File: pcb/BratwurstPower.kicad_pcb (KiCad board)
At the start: 4 copper layers, 85 x 56 mm, 142 parts, among them J1 BarrelJack, J10 GPIO, J11 OTG, J2 RaspiPower, J3 USB1in, J4 USB1out, J5 I2C, J6 I2C, J7 USB2in, J8 USB2out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

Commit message: fix: change pots to 2.2kΩ
fix: part numbers
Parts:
- Q1: value AO3401A -> HL3415A
- RV1, RV2, RV3, RV4: value 2k -> 2k2
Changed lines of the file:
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@@
 			)
 		)
+		(property "LCSC" "C52923"
+			(at 0 0 -90)
+			(unlocked yes)
+			(layer "F.Fab")
+			(hide yes)
+			(effects
+				(font
+					(size 1 1)
+					(thickness 0.15)
+				)
+			)
+		)
 		(property ki_fp_filters "C_*")
 		(sheetname "Root")
@@
 			)
 		)
-		(property "LCSC" "C25890"
+		(property "LCSC" "C25879"
 			(at 0 0 90)
 			(unlocked yes)
@@
 			)
 		)
-		(property "Value" "AO3401A"
+		(property "Value" "HL3415A"
 			(at 0 2.4 90)
 			(layer "F.Fab")
@@
 			)
 		)
-		(property "Datasheet" "http://www.aosmd.com/pdfs/datasheet/AO3401A.pdf"
+		(property "Datasheet" "https://wmsc.lcsc.com/wmsc/upload/file/pdf/v2/lcsc/2407121622_hongjiacheng-HL3415A_C28646270.pdf"
 			(at 0 0 -90)
 			(unlocked yes)
@@
 			)
 		)
-		(property "LCSC" "C15127"
+		(property "LCSC" "C28646270"
 			(at 0 0 -90)
 			(unlocked yes)
@@
 			)
 		)
-		(property "Value" "2k"
+		(property "Value" "2k2"
 			(at 0 1 180)
 			(unlocked yes)
@@
 			)
 		)
-		(property "LCSC" "C128549"
+		(property "LCSC" "C145162"
 			(at 0 0 180)
 			(unlocked yes)
@@
 			)
 		)
-		(property "LCSC" "C25765"
+		(property "LCSC" "C25762"
 			(at 0 0 0)
 			(unlocked yes)
@@
 			)
 		)
-		(property "Value" "2k"
+		(property "Value" "2k2"
 			(at 0 1 90)
 			(unlocked yes)
@@
 			)
 		)
-		(property "LCSC" "C128549"
+		(property "LCSC" "C145162"
 			(at 0 0 90)
 			(unlocked yes)
@@
 			)
 		)
+		(property "LCSC" "C52923"
+			(at 0 0 90)
+			(unlocked yes)
+			(layer "F.Fab")
+			(hide yes)
+			(effects
+				(font
+					(size 1 1)
+					(thickness 0.15)
+				)
+			)
+		)
 		(property ki_fp_filters "C_*")
 		(sheetname "Root")
@@
 			)
 		)
-		(property "Value" "2k"
+		(property "Value" "2k2"
 			(at 0 1 180)
 			(unlocked yes)
@@
 			)
 		)
-		(property "LCSC" "C128549"
+		(property "LCSC" "C145162"
 			(at 0 0 180)
 			(unlocked yes)
@@
 			)
 		)
-		(property "LCSC" "C25890"
+		(property "LCSC" "C25879"
 			(at 0 0 90)
 			(unlocked yes)
@@
 			)
 		)
+		(property "LCSC" "C5446"
+			(at 0 0 90)
+			(unlocked yes)
+			(layer "F.Fab")
+			(hide yes)
+			(effects
+				(font
+					(size 1 1)
+					(thickness 0.15)
+				)
+			)
+		)
 		(property ki_fp_filters "SOT?23?3*")
 		(sheetname "Root")
@@
 			)
 		)
-		(property "LCSC" "C25765"
+		(property "LCSC" "C25762"
 			(at 0 0 90)
 			(unlocked yes)
@@
 			)
 		)
-		(property "Value" "2k"
+		(property "Value" "2k2"
 			(at 0 1 -90)
 			(unlocked yes)
@@
 			)
 		)
-		(property "LCSC" "C128549"
+		(property "LCSC" "C145162"
 			(at 0 0 -90)
 			(unlocked yes)
@@
 			)
 		)
-		(property "LCSC" "C25765"
+		(property "LCSC" "C25762"
 			(at 0 0 -90)
 			(unlocked yes)
@@
 			)
 		)
-		(property "LCSC" "C25765"
+		(property "LCSC" "C25762"
 			(at 0 0 0)
 			(unlocked yes)

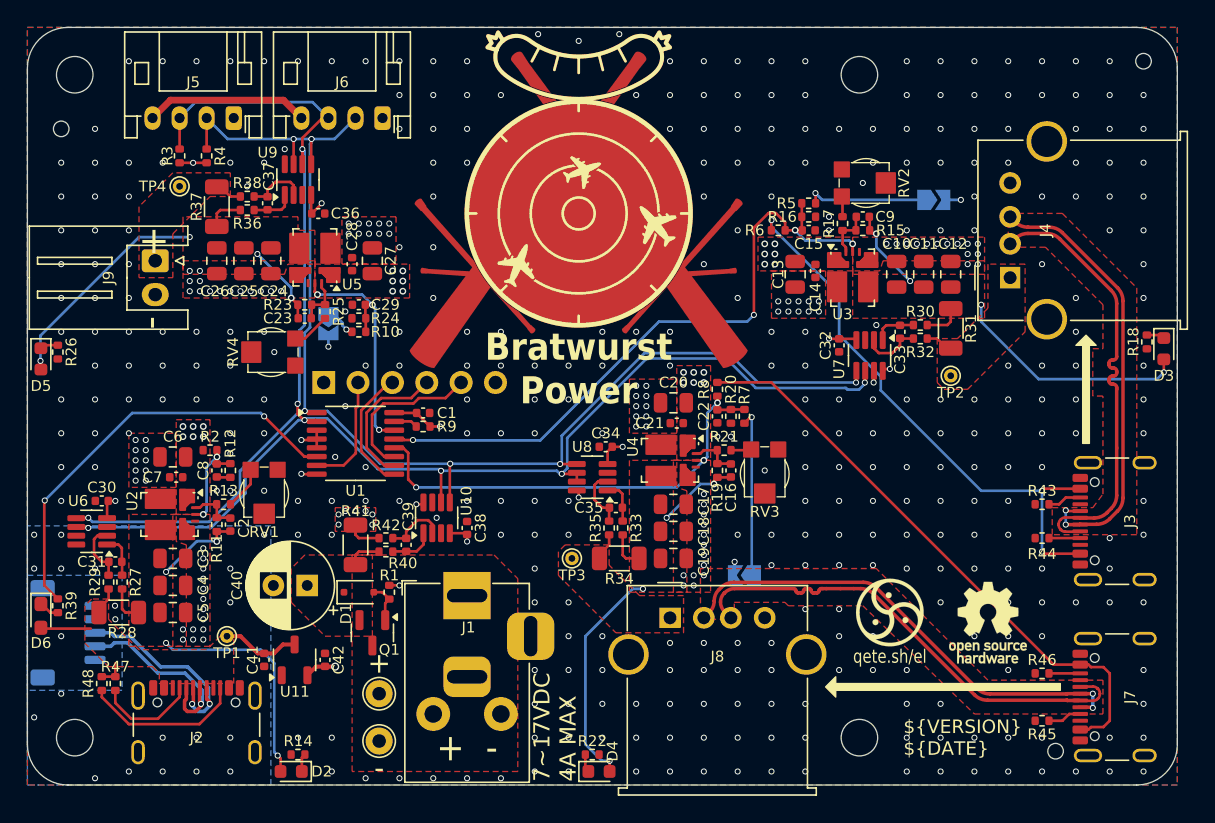
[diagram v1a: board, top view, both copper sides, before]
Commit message: fix: add thermal relief to USB ports
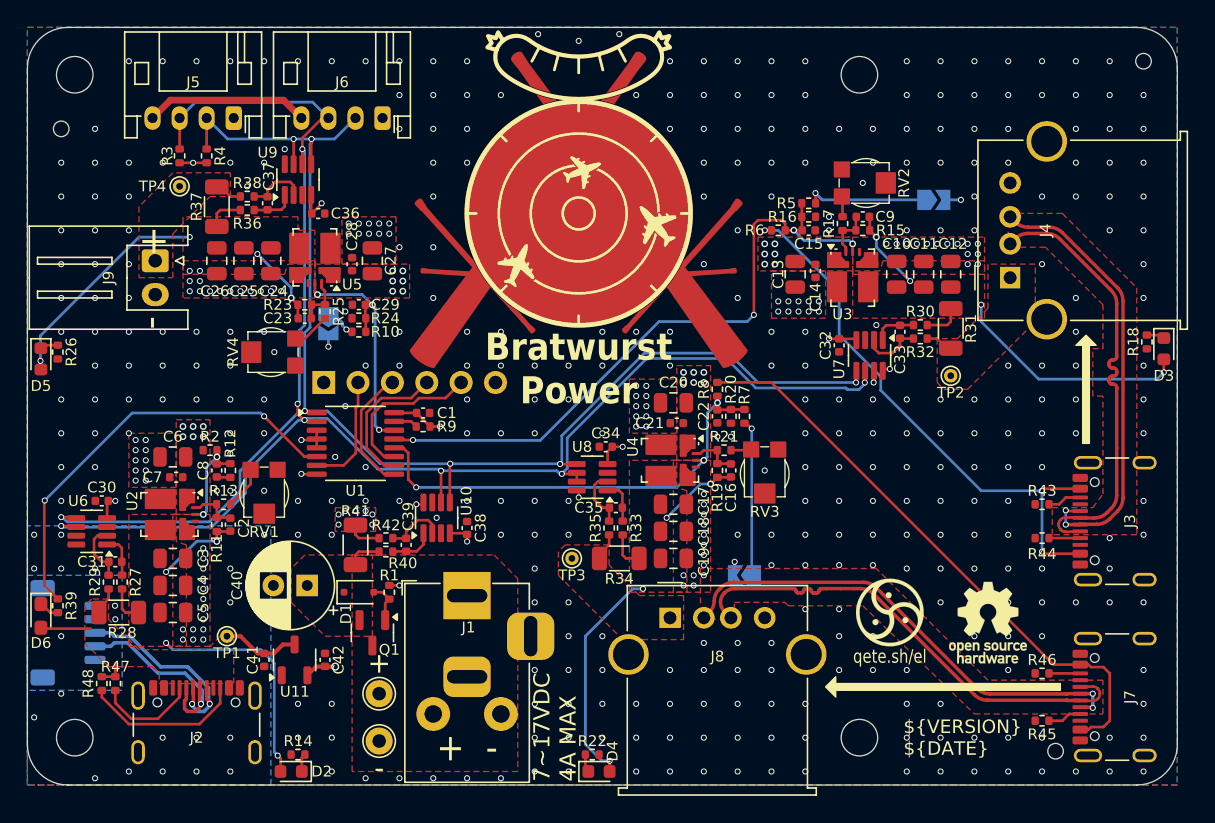
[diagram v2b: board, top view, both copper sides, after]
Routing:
- net SCL: track 113.7 -> 115.9 mm
- net SDA: track 116.7 -> 118.9 mm
- net /5Vu2EN: track 12.5 -> 11.6 mm
- net /U1en: track 49.2 -> 48.6 mm
- net GND: vias 472 -> 473

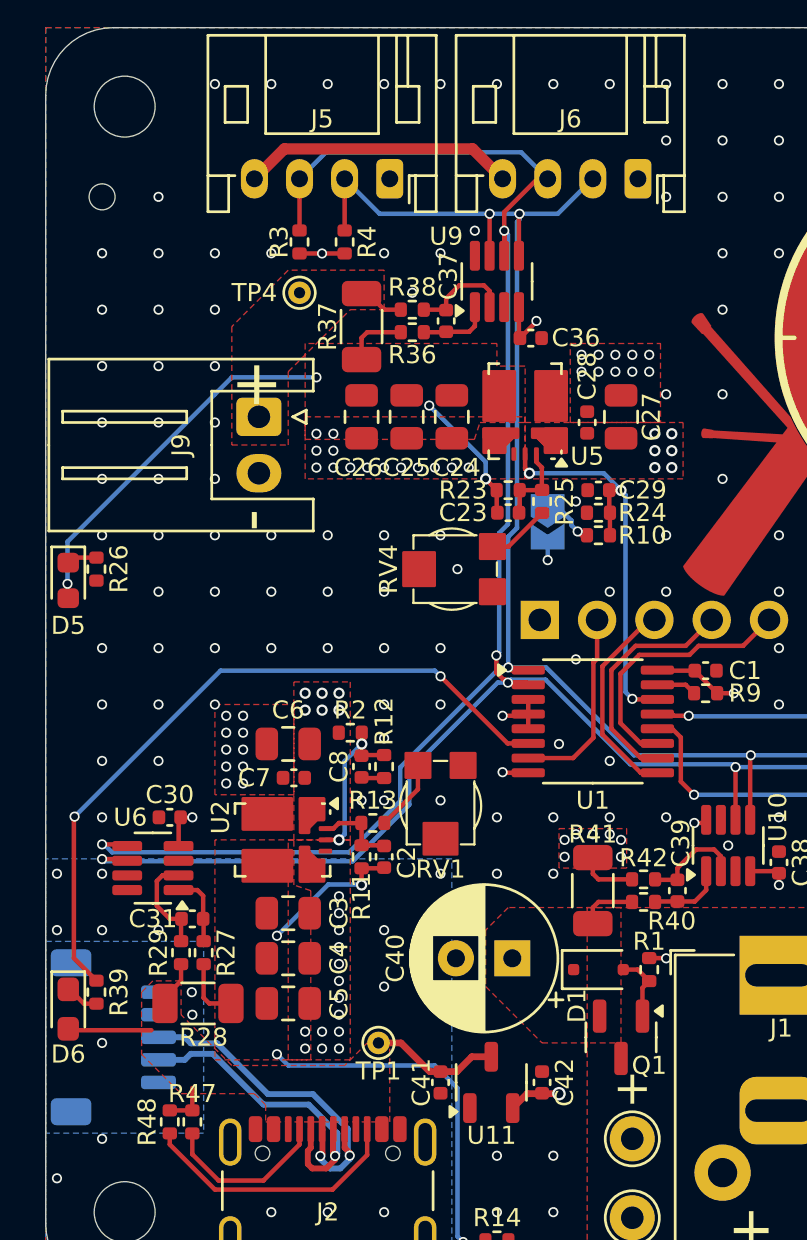
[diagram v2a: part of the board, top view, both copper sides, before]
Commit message: fix: few missing gnd vias
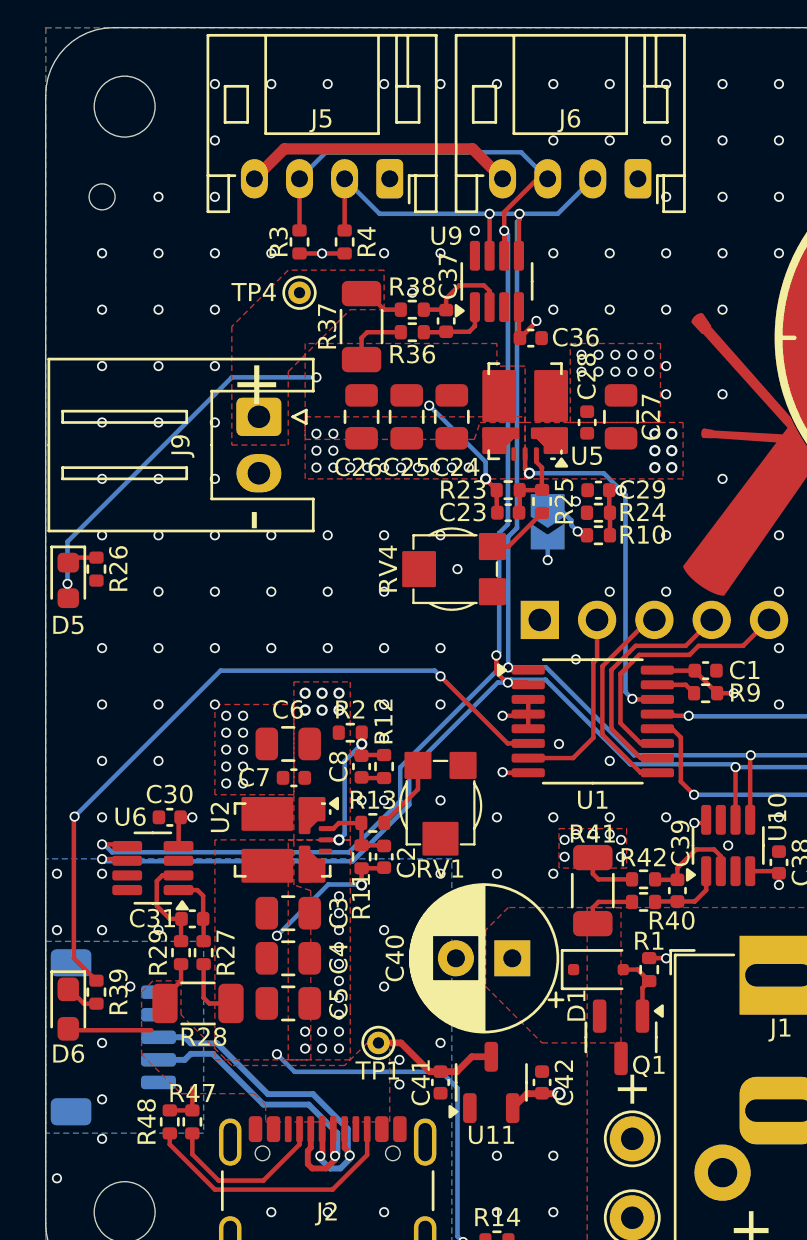
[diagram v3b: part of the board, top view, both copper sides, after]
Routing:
- net GND: vias 473 -> 487
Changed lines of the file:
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@@
 	)
 	(via
+		(at 152.5 85)
+		(size 0.45)
+		(drill 0.3)
+		(layers "F.Cu" "B.Cu")
+		(free yes)
+		(net 1)
+	)
+	(via
 		(at 135.5 113.5)
 		(size 0.45)
@@
 	)
 	(via
+		(at 143.18 125.75)
+		(size 0.45)
+		(drill 0.3)
+		(layers "F.Cu" "B.Cu")
+		(free yes)
+		(net 1)
+	)
+	(via
 		(at 177.5 82.5)
 		(size 0.45)
@@
 	)
 	(via
+		(at 135 87.5)
+		(size 0.45)
+		(drill 0.3)
+		(layers "F.Cu" "B.Cu")
+		(free yes)
+		(net 1)
+	)
+	(via
 		(at 145 102.5)
 		(size 0.45)
@@
 	)
 	(via
+		(at 152.5 92.5)
+		(size 0.45)
+		(drill 0.3)
+		(layers "F.Cu" "B.Cu")
+		(free yes)
+		(net 1)
+	)
+	(via
 		(at 177.5 85)
 		(size 0.45)
@@
 	)
 	(via
-		(at 134 123.75)
-		(size 0.45)
-		(drill 0.3)
-		(layers "F.Cu" "B.Cu")
-		(free yes)
-		(net 1)
-	)
-	(via
 		(at 180 90)
 		(size 0.45)
@@
 	)
 	(via
+		(at 145 125)
+		(size 0.45)
+		(drill 0.3)
+		(layers "F.Cu" "B.Cu")
+		(free yes)
+		(net 1)
+	)
+	(via
 		(at 190 119.75)
 		(size 0.45)
@@
 	)
 	(via
+		(at 130 127.5)
+		(size 0.45)
+		(drill 0.3)
+		(layers "F.Cu" "B.Cu")
+		(free yes)
+		(net 1)
+	)
+	(via
 		(at 183.75 101)
 		(size 0.45)
@@
 	)
 	(via
+		(at 155 95)
+		(size 0.45)
+		(drill 0.3)
+		(layers "F.Cu" "B.Cu")
+		(free yes)
+		(net 1)
+	)
+	(via
 		(at 175 105)
 		(size 0.45)
@@
 	)
 	(via
+		(at 152.5 90)
+		(size 0.45)
+		(drill 0.3)
+		(layers "F.Cu" "B.Cu")
+		(free yes)
+		(net 1)
+	)
+	(via
 		(at 200 85)
 		(size 0.45)
@@
 	)
 	(via
+		(at 143.18 126.84)
+		(size 0.45)
+		(drill 0.3)
+		(layers "F.Cu" "B.Cu")
+		(free yes)
+		(net 1)
+	)
+	(via
 		(at 190 110)
 		(size 0.45)
@@
 	)
 	(via
+		(at 135 85)
+		(size 0.45)
+		(drill 0.3)
+		(layers "F.Cu" "B.Cu")
+		(free yes)
+		(net 1)
+	)
+	(via
+		(at 155 92.5)
+		(size 0.45)
+		(drill 0.3)
+		(layers "F.Cu" "B.Cu")
+		(free yes)
+		(net 1)
+	)
+	(via
 		(at 130 120)
 		(size 0.45)
@@
 	)
 	(via
-		(at 133.975 122.75)
-		(size 0.45)
-		(drill 0.3)
-		(layers "F.Cu" "B.Cu")
-		(free yes)
-		(net 1)
-	)
-	(via
 		(at 142.5 122.5)
 		(size 0.45)
@@
 	)
 	(via
+		(at 150 92.5)
+		(size 0.45)
+		(drill 0.3)
+		(layers "F.Cu" "B.Cu")
+		(free yes)
+		(net 1)
+	)
+	(via
 		(at 155 135.5)
 		(size 0.45)
@@
 	)
 	(via
+		(at 155 90)
+		(size 0.45)
+		(drill 0.3)
+		(layers "F.Cu" "B.Cu")
+		(free yes)
+		(net 1)
+	)
+	(via
 		(at 185.25 101)
 		(size 0.45)
@@
 	)
 	(via
+		(at 131.25 122.5)
+		(size 0.45)
+		(drill 0.3)
+		(layers "F.Cu" "B.Cu")
+		(free yes)
+		(net 1)
+	)
+	(via
 		(at 132.5 87.5)
 		(size 0.45)
@@
 	)
 	(via
+		(at 150 90)
+		(size 0.45)
+		(drill 0.3)
+		(layers "F.Cu" "B.Cu")
+		(free yes)
+		(net 1)
+	)
+	(via
+		(at 150 85)
+		(size 0.45)
+		(drill 0.3)
+		(layers "F.Cu" "B.Cu")
+		(free yes)
+		(net 1)
+	)
+	(via
 		(at 197 97.5)
 		(size 0.45)
@@
 	)
 	(segment
-		(start 144.75 126)
-		(end 145.75 127)
-		(width 0.2)
-		(layer "B.Cu")
-		(net 15)
-	)
-	(segment
-		(start 137.75 125.5)
-		(end 138.25 126)
+		(start 138.53 126.28)
+		(end 145.03 126.28)
 		(width 0.2)
 		(layer "B.Cu")
@@
 	)
 	(segment
-		(start 138.25 126)
-		(end 144.75 126)
+		(start 137.75 125.5)
+		(end 138.53 126.28)
 		(width 0.2)
 		(layer "B.Cu")
@@
 	)
 	(segment
-		(start 145.75 127)
-		(end 145.75 133.575)
+		(start 145.03 126.28)
+		(end 145.75 127)
 		(width 0.2)
 		(layer "B.Cu")
@@
 		(width 0.2)
 		(layer "B.Cu")
+		(net 15)
+	)
+	(segment
+		(start 145.75 127)
+		(end 145.75 133.575)
+		(width 0.2)
+		(layer "B.Cu")

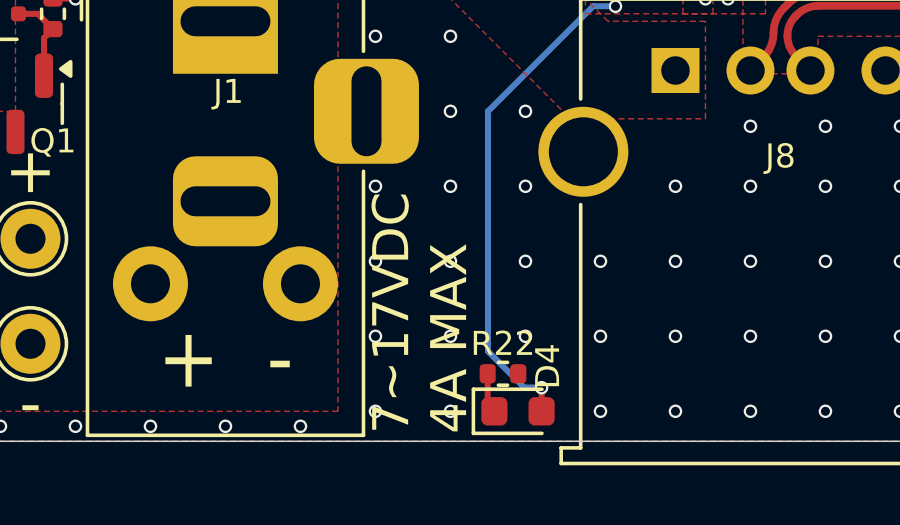
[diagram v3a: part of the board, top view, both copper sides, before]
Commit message: style: silkscreen typo
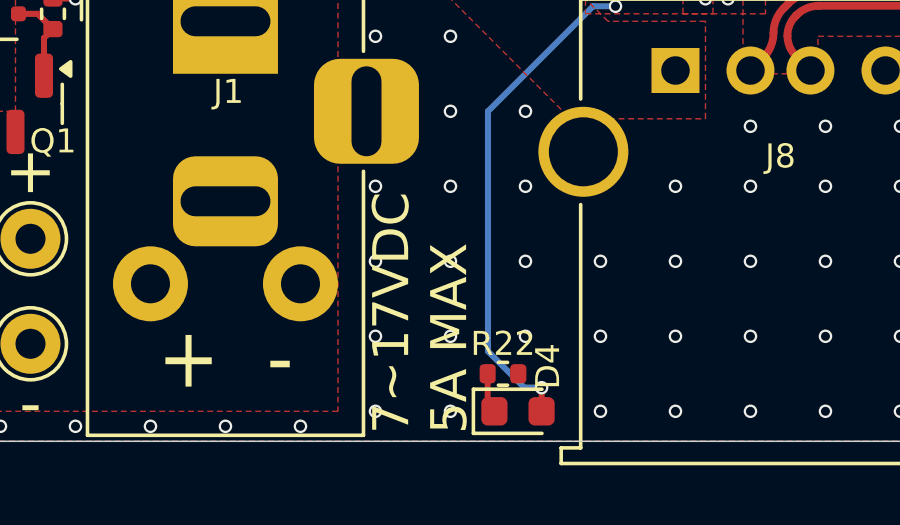
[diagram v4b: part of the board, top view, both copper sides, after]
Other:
- board text added: "7~17VDC 5A MAX"
- board text removed: "7~17VDC 4A MAX"
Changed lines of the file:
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@@
 		)
 	)
-	(gr_text "7~17VDC\n4A MAX"
+	(gr_text "7~17VDC\n5A MAX"
 		(at 166.5 135.75 90)
 		(layer "F.SilkS")
